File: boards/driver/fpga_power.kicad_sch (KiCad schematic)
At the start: 55 parts, among them J2 Barrel_Jack_Switch, J3 Conn_01x24, J4 Conn_01x24, Q87 IRF7413, U10 74LVC245, U11 74LVC245, U12 ADP151-3.3, U13 LTC4231-1, U14 74HC4514, U15 74LVC2G04, U16 74LVC2G04, U17 74LVC2G04, U18 74LVC2G04, U9 JTE0624D05

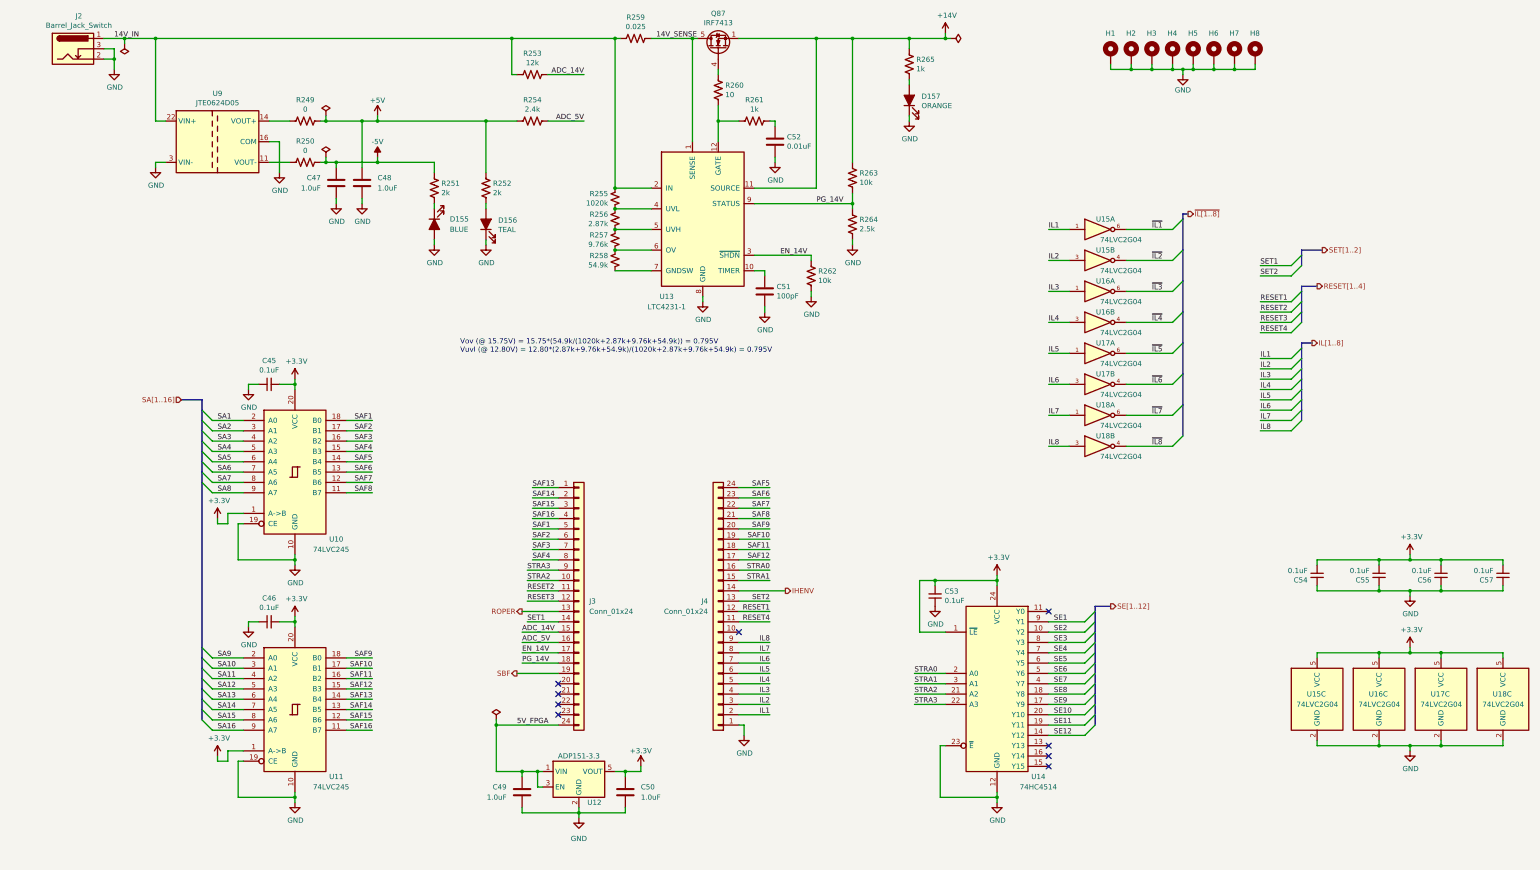
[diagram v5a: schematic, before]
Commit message: Driver: Completed preliminary placement on the top layer. <200 unwired nets to go.
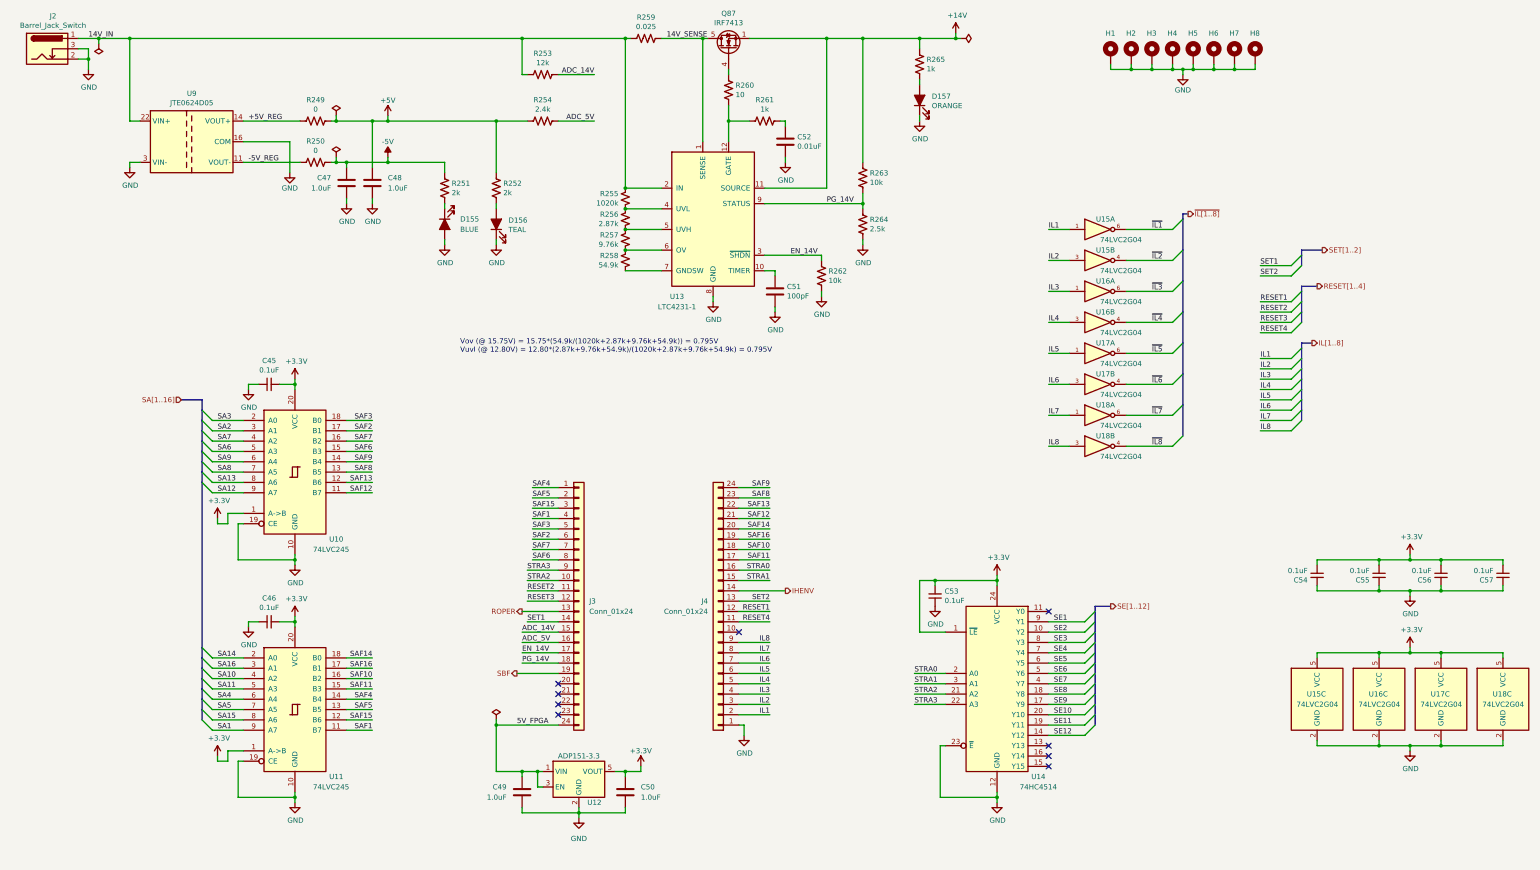
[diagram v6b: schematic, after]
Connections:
- net SA1: now also U11.9 (A7); no longer U10.2 (A0)
- net SA10: now also U11.4 (A2); no longer U11.3 (A1)
- net SA11: now also U11.5 (A3); no longer U11.4 (A2)
- net SA12: now also U10.9 (A7); no longer U11.5 (A3)
- net SA13: now also U10.8 (A6); no longer U11.6 (A4)
- net SA14: now also U11.2 (A0); no longer U11.7 (A5)
- net SA16: now also U11.3 (A1); no longer U11.9 (A7)
- net SA3: now also U10.2 (A0); no longer U10.4 (A2)
- net SA4: now also U11.6 (A4); no longer U10.5 (A3)
- net SA5: now also U11.7 (A5); no longer U10.6 (A4)
- net SA6: now also U10.5 (A3); no longer U10.7 (A5)
- net SA7: now also U10.4 (A2); no longer U10.8 (A6)
- net SA8: now also U10.7 (A5); no longer U10.9 (A7)
- net SA9: now also U10.6 (A4); no longer U11.2 (A0)
- net SAF1: now also J3.4 (Pin_4), U11.11 (B7); no longer J3.5 (Pin_5), U10.18 (B0)
- net SAF10: now also J4.18 (Pin_18), U11.16 (B2); no longer J4.19 (Pin_19), U11.17 (B1)
- net SAF11: now also J4.17 (Pin_17), U11.15 (B3); no longer J4.18 (Pin_18), U11.16 (B2)
- net SAF12: now also J4.21 (Pin_21), U10.11 (B7); no longer J4.17 (Pin_17), U11.15 (B3)
- net SAF13: now also J4.22 (Pin_22), U10.12 (B6); no longer J3.1 (Pin_1), U11.14 (B4)
- net SAF14: now also J4.20 (Pin_20), U11.18 (B0); no longer J3.2 (Pin_2), U11.13 (B5)
- net SAF16: now also J4.19 (Pin_19), U11.17 (B1); no longer J3.4 (Pin_4), U11.11 (B7)
- net SAF3: now also J3.5 (Pin_5), U10.18 (B0); no longer J3.7 (Pin_7), U10.16 (B2)
- net SAF4: now also J3.1 (Pin_1), U11.14 (B4); no longer J3.8 (Pin_8), U10.15 (B3)
- net SAF5: now also J3.2 (Pin_2), U11.13 (B5); no longer J4.24 (Pin_24), U10.14 (B4)
- net SAF6: now also J3.8 (Pin_8), U10.15 (B3); no longer J4.23 (Pin_23), U10.13 (B5)
- net SAF7: now also J3.7 (Pin_7), U10.16 (B2); no longer J4.22 (Pin_22), U10.12 (B6)
- net SAF8: now also J4.23 (Pin_23), U10.13 (B5); no longer J4.21 (Pin_21), U10.11 (B7)
- net SAF9: now also J4.24 (Pin_24), U10.14 (B4); no longer J4.20 (Pin_20), U11.18 (B0)
- net -5V_REG: now reaches R250.2, U9.11 (VOUT-)
- net +5V_REG: now reaches R249.2, U9.14 (VOUT+)
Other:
- moved on the sheet: C47, C48, C51, C52, D155, D156, D157, J2, Q87, R249, R250, R251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

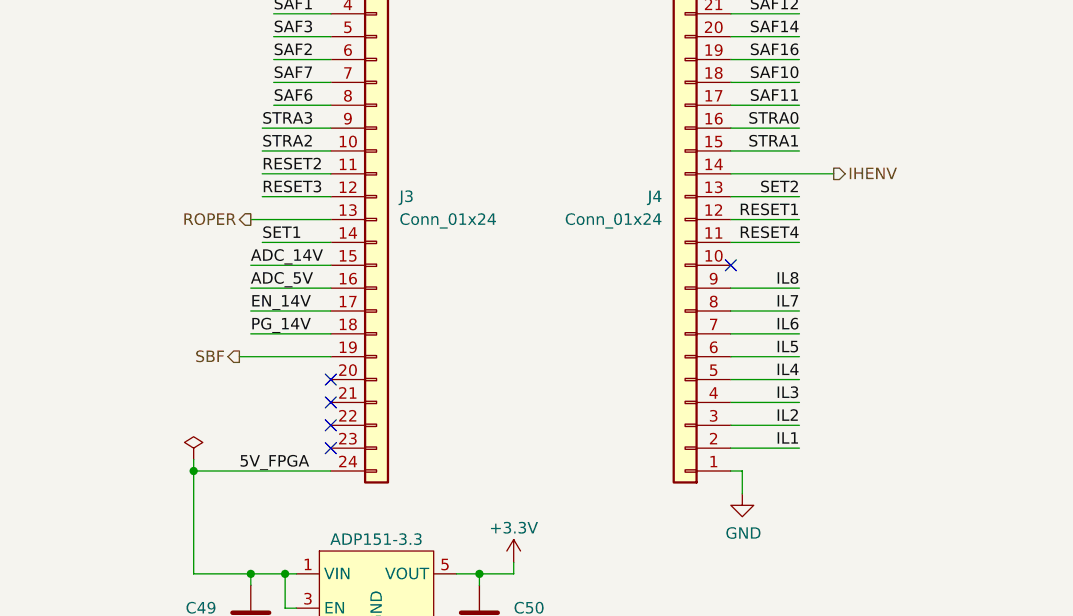
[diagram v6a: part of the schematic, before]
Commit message: Driver: a bit more routing work. May revisit 3.3V logic placement to ease contention around the FPGA
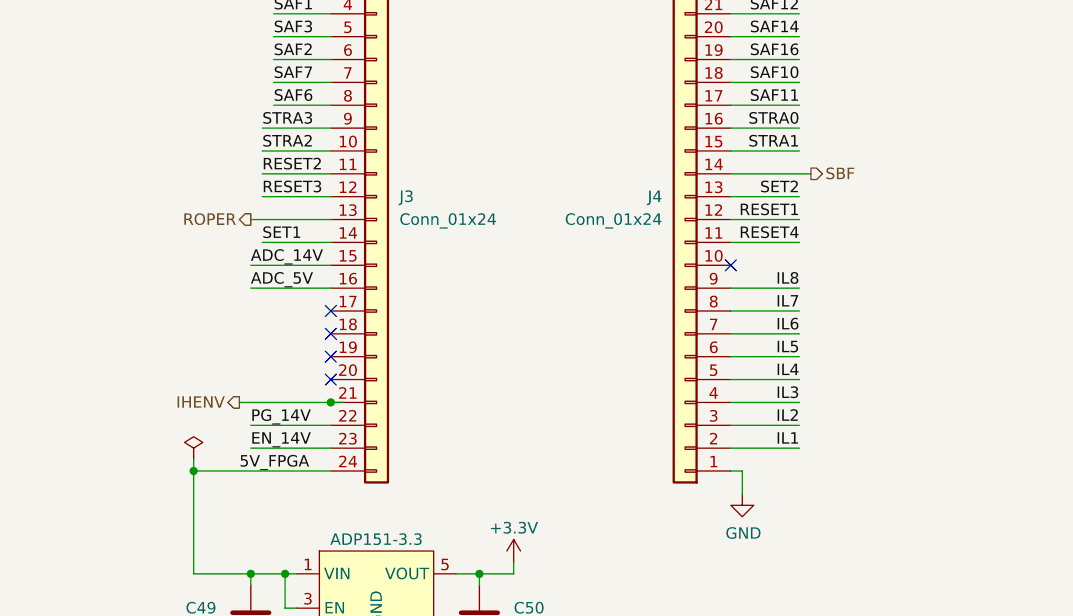
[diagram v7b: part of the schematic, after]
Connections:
- net EN_14V: now also J3.23 (Pin_23); no longer J3.17 (Pin_17)
- net IHENV: now also J3.21 (Pin_21); no longer J4.14 (Pin_14)
- net PG_14V: now also J3.22 (Pin_22); no longer J3.18 (Pin_18)
- net SBF: now also J4.14 (Pin_14); no longer J3.19 (Pin_19)
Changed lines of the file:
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@@
   (junction (at 87.63 121.92) (diameter 0) (color 0 0 0 0)
+  )
+  (junction (at 152.4 198.12) (diameter 0) (color 0 0 0 0)
   )
   (junction (at 241.3 36.83) (diameter 0) (color 0 0 0 0)
@@
   (no_connect (at 273.05 210.82))
   (no_connect (at 152.4 195.58))
-  (no_connect (at 152.4 200.66))
-  (no_connect (at 152.4 203.2))
+  (no_connect (at 152.4 193.04))
   (no_connect (at 273.05 213.36))
   (no_connect (at 196.85 182.88))
-  (no_connect (at 152.4 198.12))
+  (no_connect (at 152.4 190.5))
+  (no_connect (at 152.4 187.96))
   (no_connect (at 273.05 215.9))
   (no_connect (at 273.05 177.8))
@@
     (stroke (width 0) (type default) (color 0 0 0 0))
   )
-  (wire (pts (xy 152.4 190.5) (xy 143.51 190.5))
+  (wire (pts (xy 152.4 203.2) (xy 143.51 203.2))
     (stroke (width 0) (type default) (color 0 0 0 0))
   )
@@
     (stroke (width 0) (type default) (color 0 0 0 0))
   )
-  (wire (pts (xy 152.4 187.96) (xy 143.51 187.96))
+  (wire (pts (xy 152.4 200.66) (xy 143.51 200.66))
     (stroke (width 0) (type default) (color 0 0 0 0))
   )
@@
     (stroke (width 0) (type default) (color 0 0 0 0))
   )
+  (wire (pts (xy 152.4 198.12) (xy 142.24 198.12))
+    (stroke (width 0) (type default) (color 0 0 0 0))
+  )
   (wire (pts (xy 137.16 69.85) (xy 137.16 57.15))
     (stroke (width 0) (type default) (color 0 0 0 0))
@@
     (stroke (width 0) (type default) (color 0 0 0 0))
   )
+  (wire (pts (xy 153.67 198.12) (xy 152.4 198.12))
+    (stroke (width 0) (type default) (color 0 0 0 0))
+  )
   (wire (pts (xy 124.46 86.36) (xy 124.46 87.63))
     (stroke (width 0) (type default) (color 0 0 0 0))
@@
     (stroke (width 0) (type default) (color 0 0 0 0))
   )
-  (wire (pts (xy 196.85 172.72) (xy 208.28 172.72))
-    (stroke (width 0) (type default) (color 0 0 0 0))
-  )
   (wire (pts (xy 73.66 223.52) (xy 87.63 223.52))
     (stroke (width 0) (type default) (color 0 0 0 0))
@@
     (stroke (width 0) (type default) (color 0 0 0 0))
   )
-  (wire (pts (xy 152.4 193.04) (xy 142.24 193.04))
+  (wire (pts (xy 196.85 172.72) (xy 205.74 172.72))
     (stroke (width 0) (type default) (color 0 0 0 0))
   )
@@
     (effects (font (size 1.27 1.27)) (justify left bottom))
   )
-  (label "EN_14V" (at 143.51 187.96 0)
+  (label "EN_14V" (at 143.51 203.2 0)
     (effects (font (size 1.27 1.27)) (justify left bottom))
   )
@@
     (effects (font (size 1.27 1.27)) (justify right bottom))
   )
-  (label "PG_14V" (at 143.51 190.5 0)
+  (label "PG_14V" (at 143.51 200.66 0)
     (effects (font (size 1.27 1.27)) (justify left bottom))
   )
@@
     (effects (font (size 1.27 1.27)) (justify left bottom))
   )
-  (hierarchical_label "SBF" (shape output) (at 142.24 193.04 180)
-    (effects (font (size 1.27 1.27)) (justify right))
+  (hierarchical_label "SBF" (shape output) (at 205.74 172.72 0)
+    (effects (font (size 1.27 1.27)) (justify left))
   )
   (hierarchical_label "RESET[1..4]" (shape output) (at 339.09 97.79 0)
@@
     (effects (font (size 1.27 1.27)) (justify left))
   )
+  (hierarchical_label "IHENV" (shape output) (at 142.24 198.12 180)
+    (effects (font (size 1.27 1.27)) (justify right))
+  )
   (hierarchical_label "SE[1..12]" (shape output) (at 288.29 176.53 0)
     (effects (font (size 1.27 1.27)) (justify left))
@@
     (effects (font (size 1.27 1.27)) (justify right))
   )
-  (hierarchical_label "IHENV" (shape output) (at 208.28 172.72 0)
-    (effects (font (size 1.27 1.27)) (justify left))
-  )
   (hierarchical_label "ROPER" (shape output) (at 143.51 177.8 180)
